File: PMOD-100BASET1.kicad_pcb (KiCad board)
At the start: 4 copper layers, 102 x 44 mm, 115 parts, among them J1 Conn_01x02, J2 RB1-125B8G1A, J3 2304372-1, J4 Conn_01x02, J5 Tag Connect SWD, P1 USB_C_Plug_USB2.0, Q1 AO3401A, Q2 AO3400A, Q3 AO3401A, Q4 AO3400A, SW1 Reset, SW2 Boot, U1 AP1117-33, U2 STM32F072CBTx, U3 24LC16, U4 DP83TC813RRHFRQ1, U5 LAN8720A, Y1 25MHz

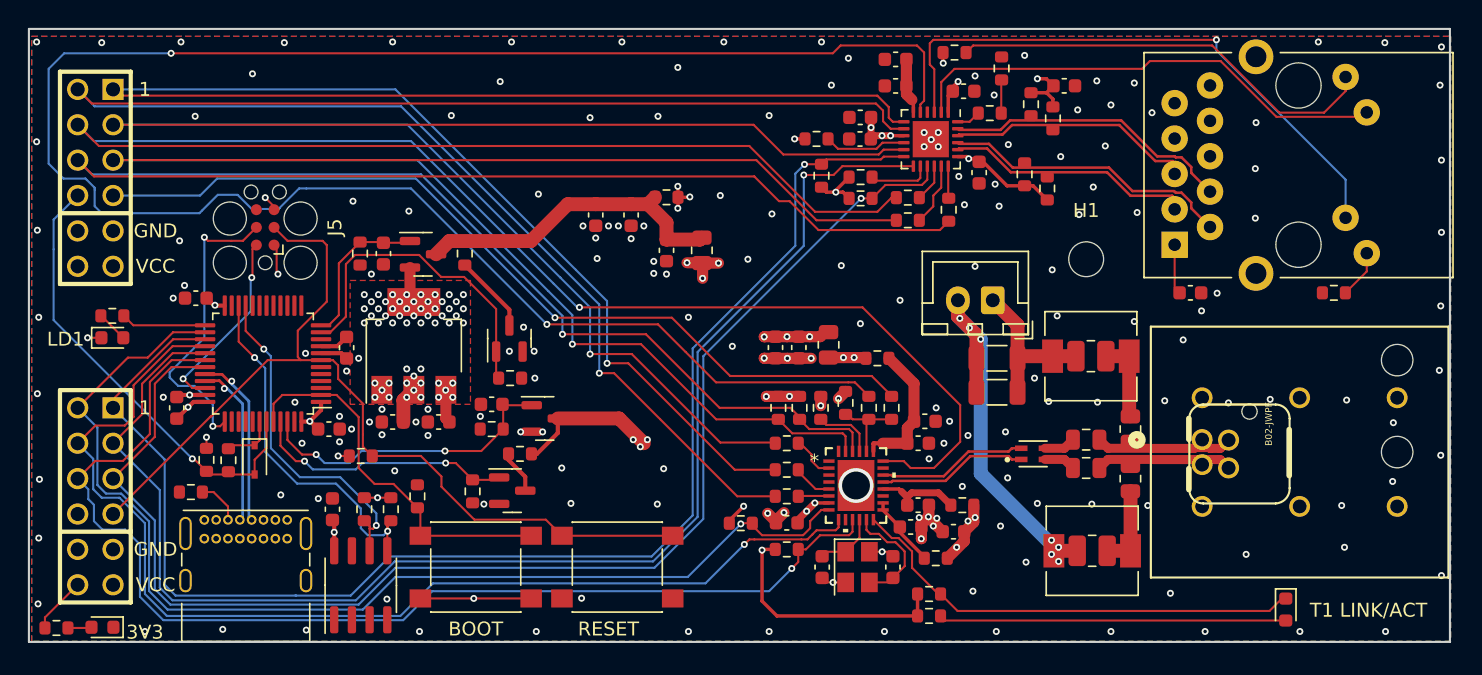
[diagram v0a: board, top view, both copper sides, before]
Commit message: [doc] added readme; updated files to Kicad V8
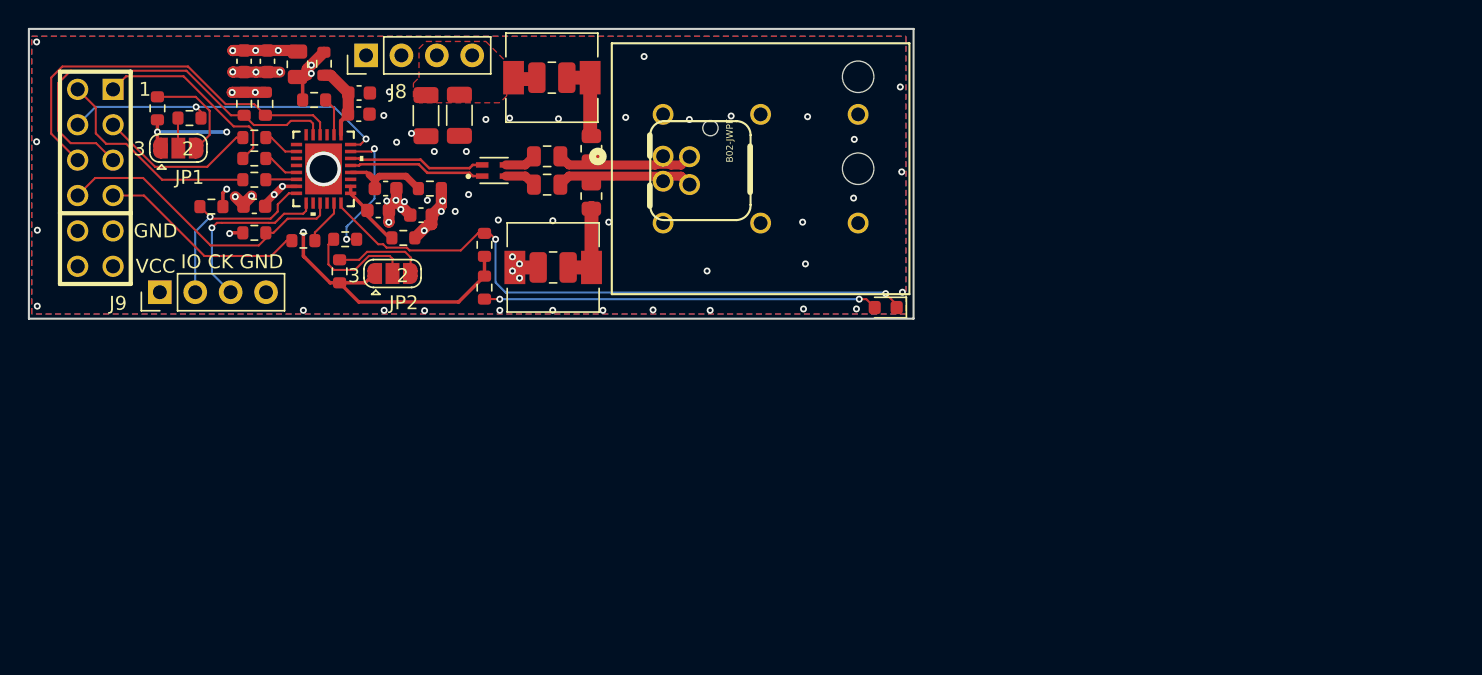
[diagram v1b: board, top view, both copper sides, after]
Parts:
- removed C1, C10, C17, C2, C22, C28: 4.7u, Capacitor_SMD:C_0603_1608Metric
- removed C12, C14, C23, C24, C27, C29, C3, C30, C31, C32, C6: 100n, Capacitor_SMD:C_0603_1608Metric
- removed C15, C4, C5: 10p, Capacitor_SMD:C_0603_1608Metric
- removed C19: 470p, Capacitor_SMD:C_0603_1608Metric
- removed C21: 20p, Capacitor_SMD:C_0603_1608Metric
- removed D1: 1N5819, Diode_SMD:D_SOD-323
- removed FB2: 100@100M, Resistor_SMD:R_0805_2012Metric
- removed H1: MountingHole, MountingHole:MountingHole_2.5mm
- removed J2: RB1-125B8G1A, Connector_RJ:RJ45_UDE_RB1-125B8G1A
- removed J4: Conn_01x02, Connector_JST:JST_XH_B2B-XH-A_1x02_P2.50mm_Vertical
- removed J5: Tag Connect SWD, Connector:Tag-Connect_TC2030-IDC-FP_2x03_P1.27mm_Vertical
- removed LD1: YELLOW, LED_SMD:LED_0603_1608Metric
- removed LD2: RED, LED_SMD:LED_0603_1608Metric
- removed P1: USB_C_Plug_USB2.0, Connector_USB:USB_C_Receptacle_GCT_USB4085
- removed PMOD2: PMOD-Device-x2-Type-1A-GPIO, pmod-conn_6x2:pmod_pin_array_6x2
- removed Q1, Q3: AO3401A, Package_TO_SOT_SMD:SOT-23
- removed Q2, Q4: AO3400A, Package_TO_SOT_SMD:SOT-23
- removed R10, R11, R18, R19, R22, R38, R45, R47, R8, R9: 1k, Resistor_SMD:R_0603_1608Metric
- removed R17, R24, R25, R26, R27, R34: 10, Resistor_SMD:R_0603_1608Metric
- removed R20, R21, R23, R43, R5, R6: 2.4k, Resistor_SMD:R_0603_1608Metric
- removed R29: 0, Resistor_SMD:R_0603_1608Metric
- removed R31, R32, R33, R36: 49.9, Resistor_SMD:R_0603_1608Metric
- removed R37: 12k, Resistor_SMD:R_0603_1608Metric
- removed R7: 5.1k, Resistor_SMD:R_0603_1608Metric
- removed SW1: Reset, Button_Switch_SMD:SW_Push_1P1T_NO_6x6mm_H9.5mm
- removed SW2: Boot, Button_Switch_SMD:SW_Push_1P1T_NO_6x6mm_H9.5mm
- removed U1: AP1117-33, Package_TO_SOT_SMD:SOT-223-3_TabPin2
- removed U2: STM32F072CBTx, Package_QFP:LQFP-48_7x7mm_P0.5mm
- removed U3: 24LC16, Package_SO:SOIC-8_3.9x4.9mm_P1.27mm
- removed U5: LAN8720A, Package_DFN_QFN:QFN-24-1EP_4x4mm_P0.5mm_EP2.6x2.6mm
- removed Y1: 25MHz, Crystal:Crystal_SMD_3225-4Pin_3.2x2.5mm
- added J8: Conn_01x03, Connector_PinHeader_2.54mm:PinHeader_1x04_P2.54mm_Vertical, F.Cu at (84.2, 50.9)
- added J9: Conn_01x03, Connector_PinHeader_2.54mm:PinHeader_1x04_P2.54mm_Vertical, F.Cu at (69.4, 67.9)
- added JP1: SolderJumper_3_Open, Jumper:SolderJumper-3_P1.3mm_Open_RoundedPad1.0x1.5mm, F.Cu at (70.7, 57.6)
- added JP2: SolderJumper_3_Open, Jumper:SolderJumper-3_P1.3mm_Open_RoundedPad1.0x1.5mm, F.Cu at (86.1, 66.6)
- LD3: value BLUE -> WHITE
- R1: value 2.4k -> 4.7k
- R2, R4: value 2.4k -> 9.1k
- R3: value 10 -> 4.7k
- moved C11 46.9 mm to (83.7, 53.6)
- moved C13 46.6 mm to (83.7, 55.1)
- moved R28 45.0 mm to (81.2, 51.5), turned to -90 degrees
- moved R30 44.6 mm to (86.9, 64.0)
- moved C33 44.5 mm to (88.5, 55.2), turned to -90 degrees
- moved C20 44.5 mm to (85.6, 60.5)
- moved R39 44.5 mm to (88.8, 60.5)
- moved U4 44.5 mm to (81.1, 59.1)
- moved C16 44.5 mm to (85.1, 62.0)
- moved C18 44.5 mm to (88.1, 62.4)
- moved C9 44.5 mm to (76.2, 61.7)
- moved R12 44.5 mm to (76.2, 63.6)
- moved R16 44.5 mm to (76.2, 59.8)
- moved R13 44.3 mm to (73.1, 61.8), turned to 0 degrees
- moved R15 44.3 mm to (76.2, 58.3)
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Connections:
- net Net-(J4-Pin_1) renamed /V_P
- C18 pad 2: /VDD_T1 -> +3V3
- C33 pad 2: Net-(J4-Pin_2) -> GND
- C34 pad 2: Net-(J4-Pin_2) -> GND
- C7 pad 2: /VDD_T1 -> +3V3
- C8 pad 2: /VDD_T1 -> +3V3
- FB1 pad 1: /VDD_T1 -> +3V3
- L4 pad 1: Net-(J4-Pin_2) -> GND
- L5 pad 1: Net-(J4-Pin_2) -> GND
- PMOD1 pad 10: /TRX_STM -> /RST_T1
- PMOD1 pad 4: /REFCLK_PMOD -> /REFCLK
- R1 pad 1: /TRX_STM -> /RX_DV
- R1 pad 2: +3V3 -> Net-(JP1-C)
- R2 pad 1: /SDA -> Net-(JP1-B)
- R2 pad 2: +3V3 -> /VDDIO
- R3 pad 1: /U1_TX -> /RXER
- R3 pad 2: /TRX_STM -> Net-(JP2-C)
- R30 pad 1: /VDD_T1 -> +3V3
- R35 pad 1: /REFCLK_PMOD -> Net-(U4-XI)
- R35 pad 2: /RX_D3 -> /REFCLK
- R39 pad 1: /VDD_T1 -> +3V3
- R4 pad 1: /SCL -> Net-(JP2-B)
- R4 pad 2: +3V3 -> /VDDIO
- U4 pad 12: Net-(U4-XO) -> unconnected-(U4-XO-Pad12)
- U4 pad 21: unconnected-(U4-RXER-Pad21) -> /RXER
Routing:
- net /REFCLK_T: track 143.8 -> 0.00 mm, vias 2 -> 0
- net /RX_DV: track 142.6 -> 24.4 mm, vias 1 -> 2
- net /TX_D0: track 126.0 -> 15.6 mm, vias 1 -> 0
- net /TXEN: track 116.8 -> 11.4 mm, vias 1 -> 0
- net /TX_D1: track 119.6 -> 14.4 mm, vias 1 -> 0
- net /RX_D1: track 130.8 -> 28.9 mm, vias 1 -> 0
- net /MDIO_T: track 99.7 -> 0.00 mm, vias 1 -> 0
- net /MDC_T: track 99.6 -> 0.00 mm, vias 1 -> 0
- net /RST_T: track 97.7 -> 0.00 mm, vias 1 -> 0
- net /RX_D0: track 121.1 -> 29.5 mm, vias 1 -> 0
- net /MDC_T1: track 80.6 -> 13.0 mm
- net /MDIO_T1: track 80.7 -> 14.2 mm
- net /RST_STM: track 66.3 -> 0.00 mm
- net /REFCLK_PMOD: track 62.9 -> 0.00 mm, vias 1 -> 0
- net /RST_T1: track 82.0 -> 21.9 mm, vias 1 -> 0
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- added copper zone on F.Cu, net /V_P
- removed copper zone on F.Cu, net +3V3
- removed copper zone on In2.Cu, net +5V
- removed copper zone on In2.Cu, net /VDDA_T
- removed copper zone on In2.Cu, net /VDDIO_T
- removed copper zone on In2.Cu, net /VDD_T1
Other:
- board size 102 x 44 mm -> 63.5 x 20.8 mm
- board text added: "3 2"
- board text added: "IO CK GND"
- board text removed: "3V3"
- board text removed: "BOOT"
- board text removed: "LD1"
- board text removed: "RESET"
- board text removed: "T1 LINK/ACT"
